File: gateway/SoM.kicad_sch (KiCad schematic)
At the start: 20 parts, among them SW901 Reset, SW902 On / Off, X901 UART, X902 SoM

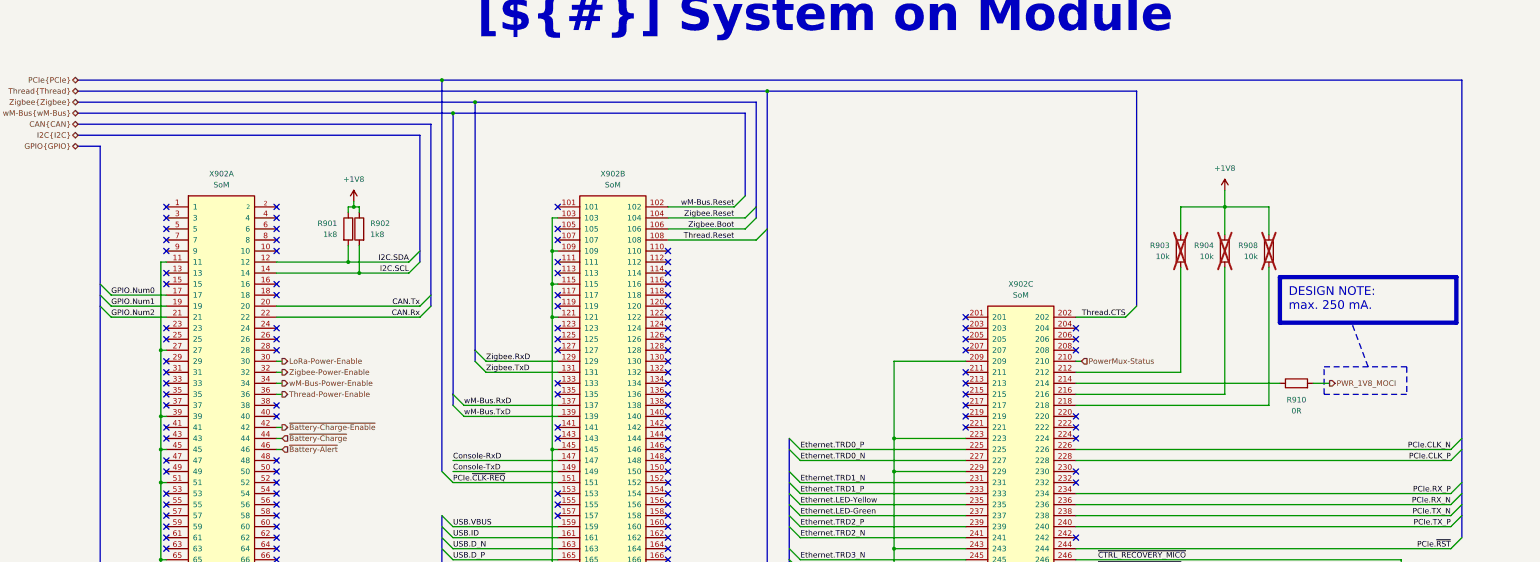
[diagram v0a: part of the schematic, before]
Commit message: Add ready LED, swap Zigbee and Console UART
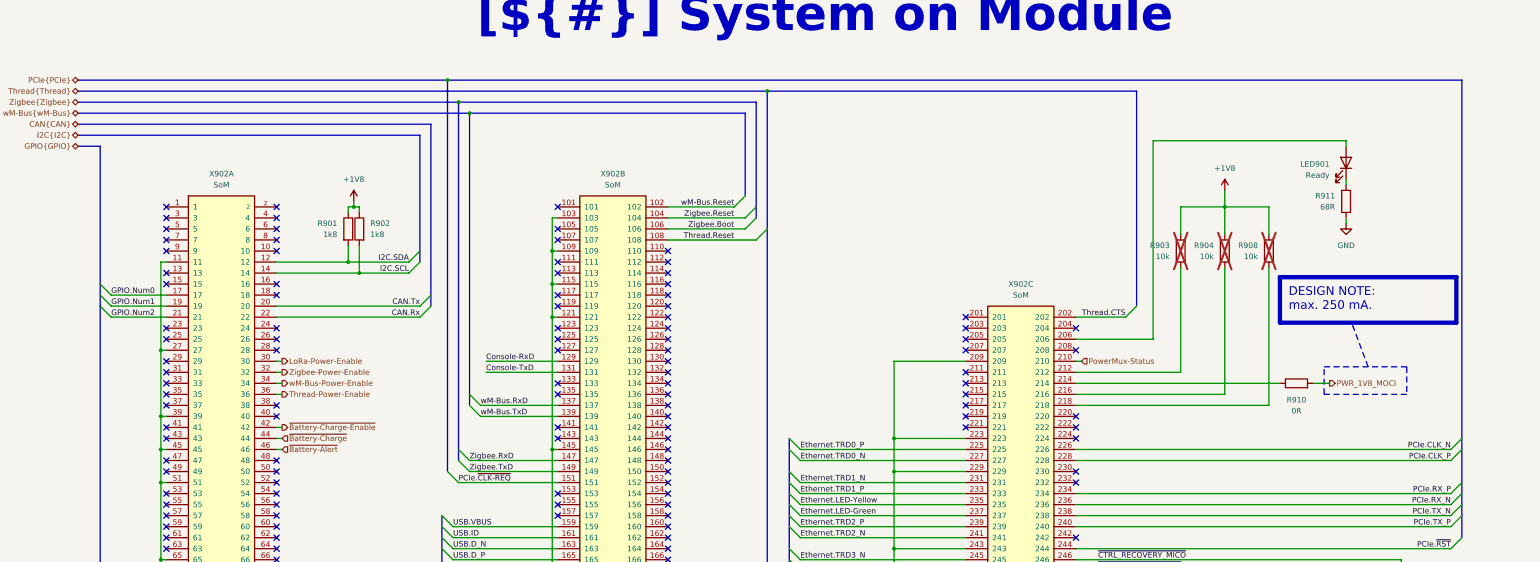
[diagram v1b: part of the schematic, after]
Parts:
- added LED901: Ready, LED_SMD:LED_0805_2012Metric, symbol Device:LED
- added R911: 68R, Resistor_SMD:R_0805_2012Metric, symbol Device:R
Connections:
- net Console-RxD: now also X902.129; no longer X902.147
- net Console-TxD: now also X902.131; no longer X902.149
- net GND: now also R911.2
- net Zigbee.RxD: now also X902.147; no longer X902.129
- net Zigbee.TxD: now also X902.149; no longer X902.131
- net at X902.206: now also LED901.2 (A)
- new net: LED901.1 (K), R911.1
- no-connect marks 159 -> 158

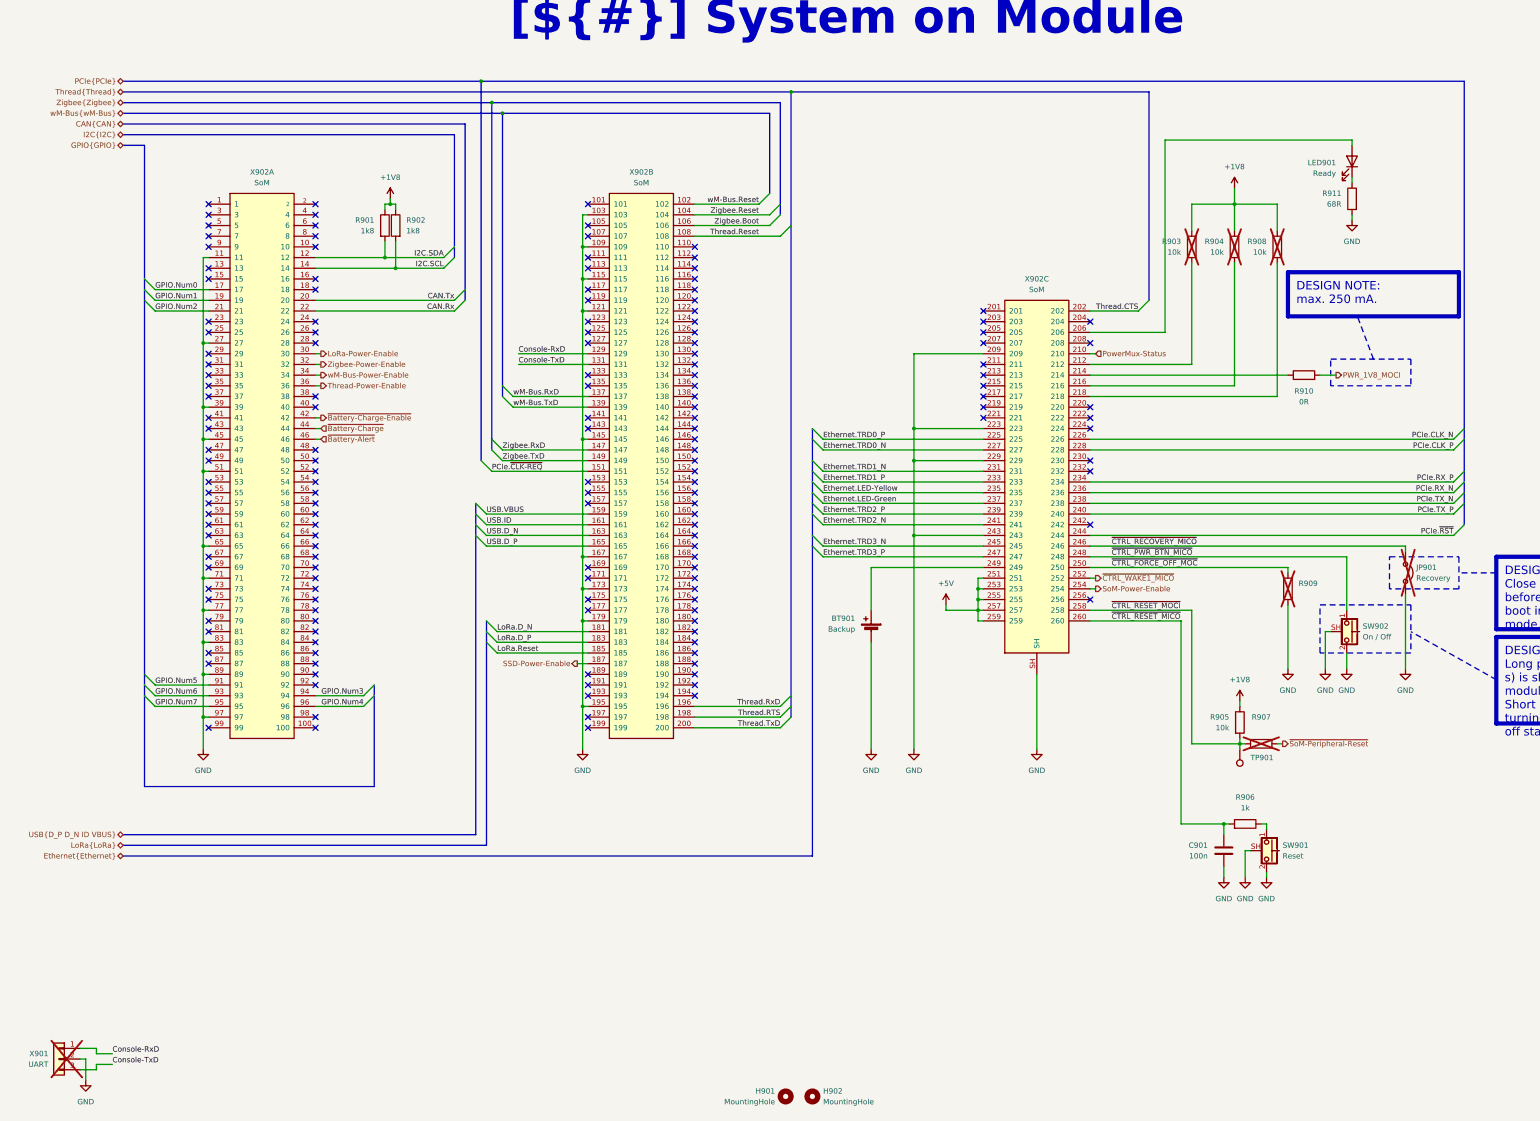
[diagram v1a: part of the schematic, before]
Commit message: Add INA219 for current measurement
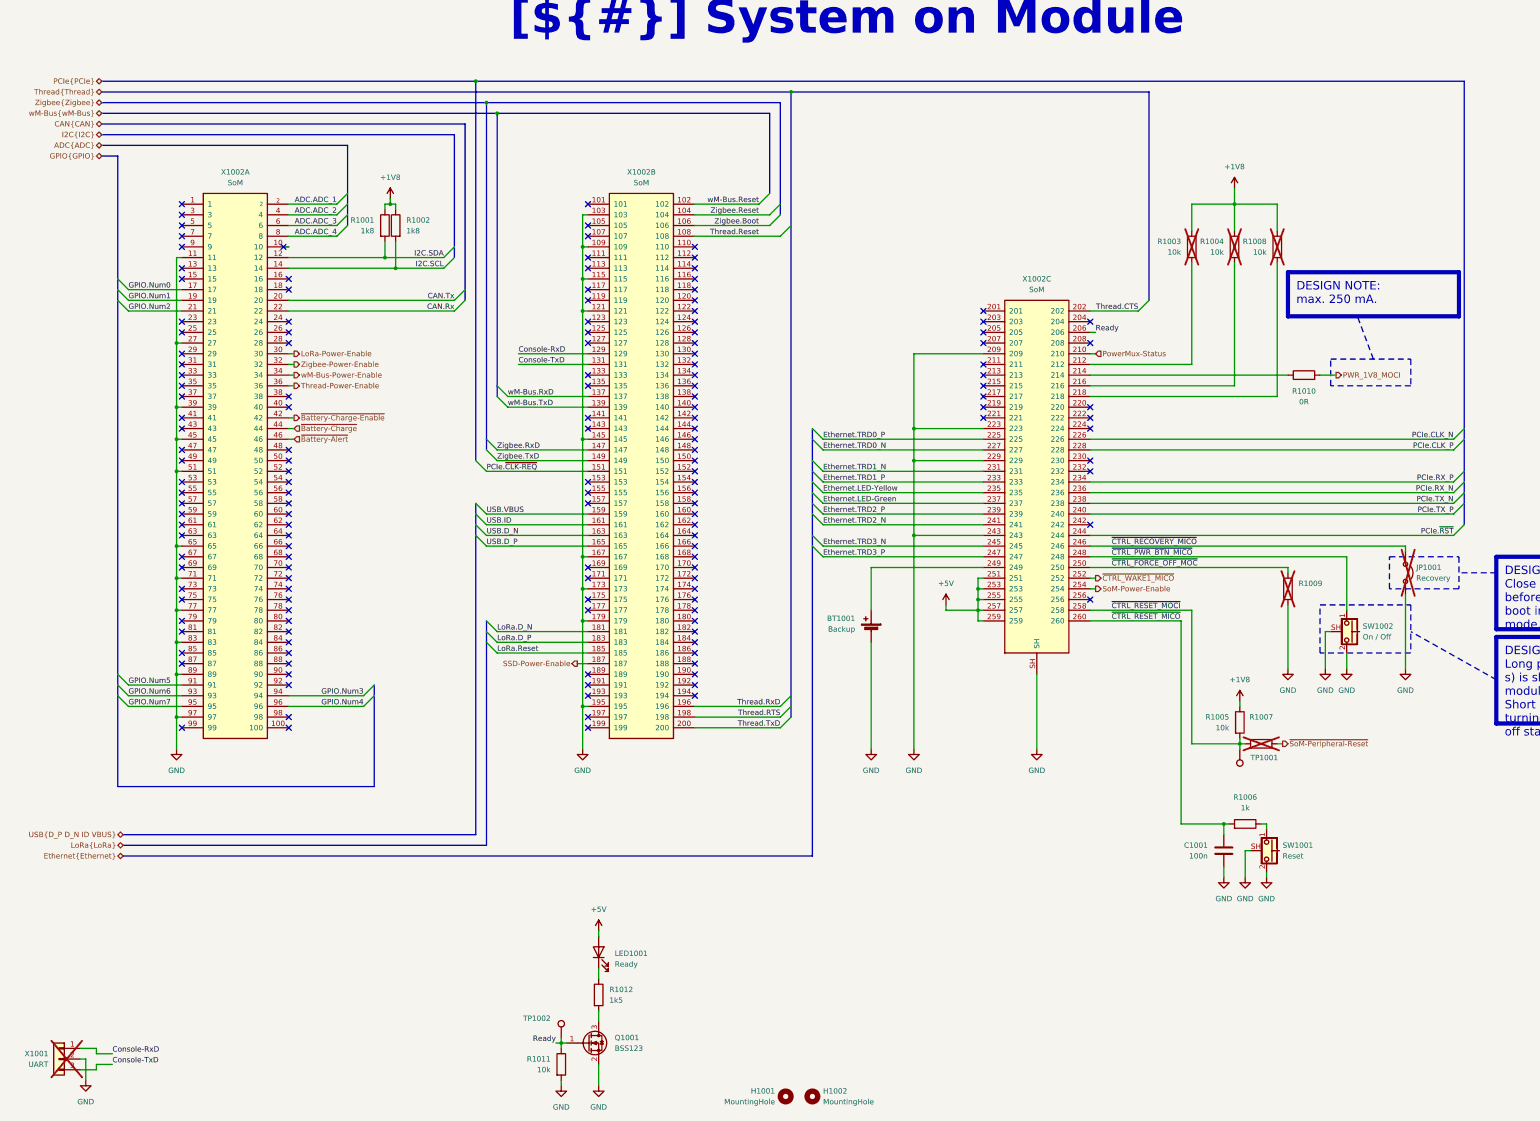
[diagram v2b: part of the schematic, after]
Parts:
- removed LED901: Ready, LED_SMD:LED_0805_2012Metric, symbol Device:LED
- removed R911: 68R, Resistor_SMD:R_0805_2012Metric, symbol Device:R
- added LED1001: Ready, LED_SMD:LED_0805_2012Metric, symbol Device:LED
- added Q1001: BSS123, Package_TO_SOT_SMD:SOT-23, symbol Transistor_FET:BSS123
- added R1011: 10k, Resistor_SMD:R_0805_2012Metric, symbol Device:R
- added R1012: 1k5, Resistor_SMD:R_0805_2012Metric, symbol Device:R
- added TP1002: ~, Testpoints_Kampi:TestPoint_Pad_1.0x1.0mm, symbol Connector:TestPoint
- renumbered BT901 to BT1001, C901 to C1001, H901 to H1001, H902 to H1002, JP901 to JP1001, R901 to R1001, R902 to R1002, R903 to R1003, R904 to R1004, R905 to R1005, R906 to R1006, R907 to R1007, R908 to R1008, R909 to R1009, R910 to R1010, SW901 to SW1001, SW902 to SW1002, TP901 to TP1001, X901 to X1001, X902 to X1002
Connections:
- net +5V: now also LED1001.2 (A)
- net GND: now also Q1001.2 (S), R1011.2
- net ADC.ADC_1: now reaches X1002.2
- net ADC.ADC_2: now reaches X1002.4
- net ADC.ADC_3: now reaches X1002.6
- net ADC.ADC_4: now reaches X1002.8
- net Ready: now reaches X1002.206
- net Ready: now also Q1001.1 (G), R1011.1, TP1002.1
- new net: Q1001.3 (D), R1012.2
- new net: LED1001.1 (K), R1012.1
- no-connect marks 158 -> 154
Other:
- moved on the sheet: X1002A

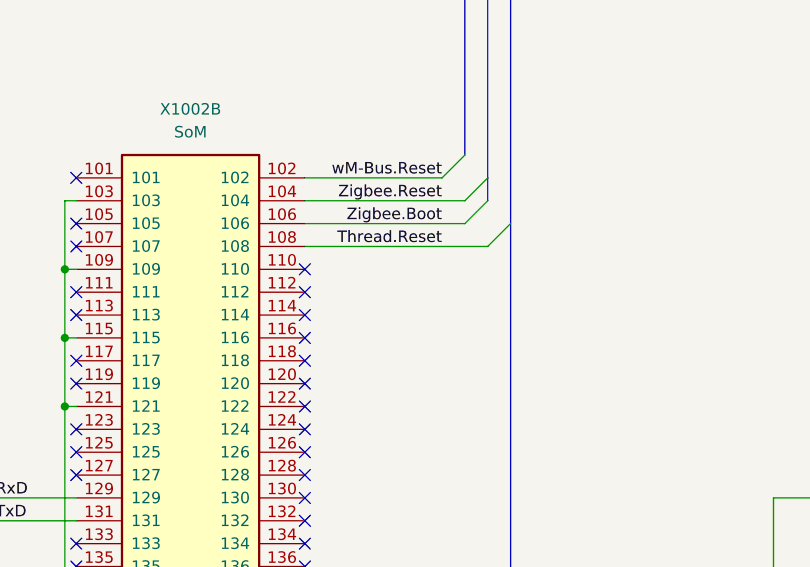
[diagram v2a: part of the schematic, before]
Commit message: Add boot signal for Thread MCU
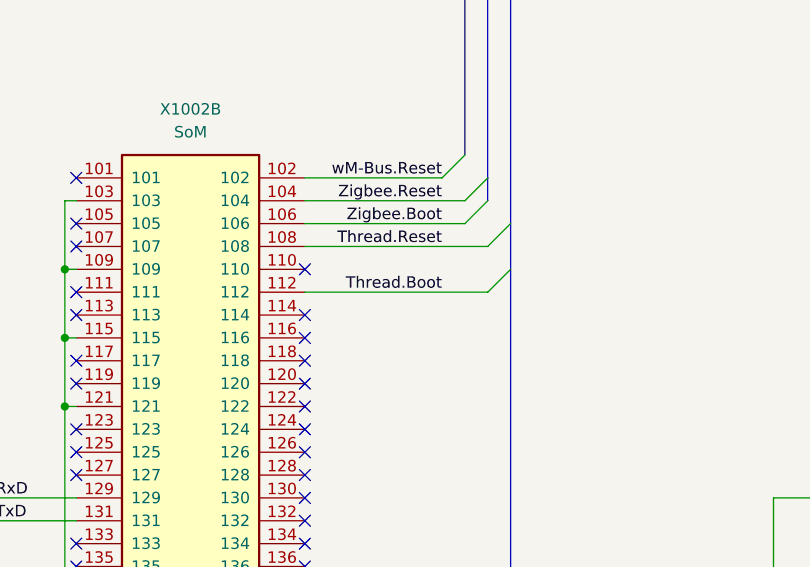
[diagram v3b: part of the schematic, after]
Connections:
- net Thread.Boot: now reaches X1002.112
- no-connect marks 154 -> 153
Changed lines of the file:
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@@
 	)
 	(no_connect
-		(at 173.99 80.01)
-	)
-	(no_connect
 		(at 52.07 118.11)
 	)
@@
 	)
 	(bus_entry
+		(at 196.85 77.47)
+		(size -2.54 2.54)
+		(stroke
+			(width 0)
+			(type default)
+		)
+	)
+	(bus_entry
 		(at 124.46 166.37)
 		(size 2.54 2.54)
@@
 	(wire
 		(pts
+			(xy 173.99 80.01) (xy 194.31 80.01)
+		)
+		(stroke
+			(width 0)
+			(type default)
+		)
+	)
+	(wire
+		(pts
 			(xy 77.47 107.95) (xy 78.74 107.95)
 		)
@@
 		)
 	)
+	(label "Thread.Boot"
+		(at 189.23 80.01 180)
+		(effects
+			(font
+				(size 1.27 1.27)
+			)
+			(justify right bottom)
+		)
+	)

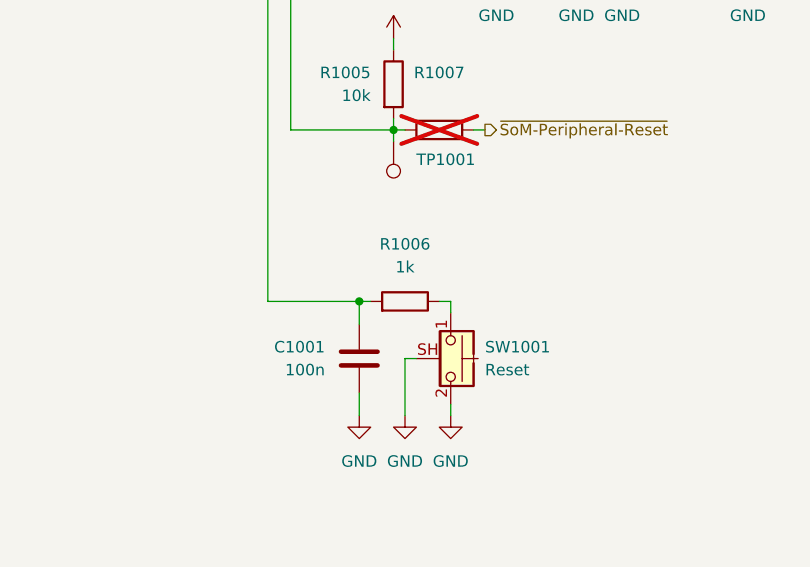
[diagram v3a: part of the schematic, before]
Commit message: Improving Thread
- Add boot signal for Thread MCU
- Add debug LED for nRF5340
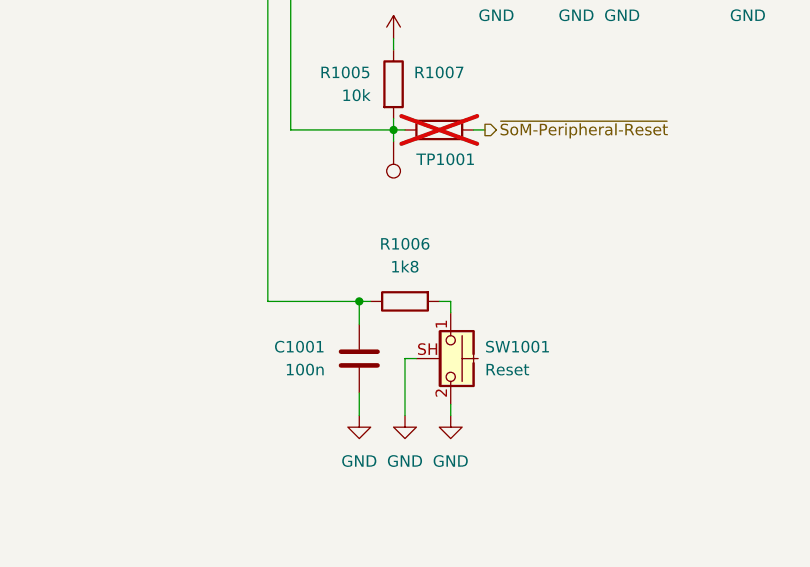
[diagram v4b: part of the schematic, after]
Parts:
- R1006: value 1k -> 1k8; manf# CR0805-FX-1001GLF -> CR0805-FX-1801GLF; mouser# 652-CR0805-FX-1001GLF -> 652-CR0805-FX-1801GLF
- TP1001, TP1002: value ~ -> (none)
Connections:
- net ~{CTRL_RESET_MICO}: now also R1006.1; no longer R1006.2
- net at SW1001.1: now also R1006.2; no longer R1006.1
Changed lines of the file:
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@@
 	)
 	(symbol
-		(lib_id "Device:R")
-		(at 304.8 214.63 270)
-		(mirror x)
-		(unit 1)
-		(body_style 1)
-		(exclude_from_sim no)
-		(in_bom yes)
-		(on_board yes)
-		(in_pos_files yes)
-		(dnp no)
-		(fields_autoplaced yes)
-		(property "Reference" "R1006"
-			(at 304.8 208.28 90)
-			(show_name no)
-			(do_not_autoplace no)
-			(effects
-				(font
-					(size 1.27 1.27)
-				)
-			)
-		)
-		(property "Value" "1k"
-			(at 304.8 210.82 90)
-			(show_name no)
-			(do_not_autoplace no)
-			(effects
-				(font
-					(size 1.27 1.27)
-				)
-			)
-		)
-		(property "Footprint" "Resistor_SMD:R_0805_2012Metric"
-			(at 304.8 216.408 90)
-			(hide yes)
-			(show_name no)
-			(do_not_autoplace no)
-			(effects
-				(font
-					(size 1.27 1.27)
-				)
-			)
-		)
-		(property "Datasheet" "https://www.mouser.de/datasheet/3/40/1/cr.pdf"
-			(at 304.8 214.63 0)
-			(hide yes)
-			(show_name no)
-			(do_not_autoplace no)
-			(effects
-				(font
-					(size 1.27 1.27)
-				)
-			)
-		)
-		(property "Description" "Resistor"
-			(at 304.8 214.63 0)
-			(hide yes)
-			(show_name no)
-			(do_not_autoplace no)
-			(effects
-				(font
-					(size 1.27 1.27)
-				)
-			)
-		)
-		(property "manf" "Bourns"
-			(at 304.8 214.63 0)
-			(hide yes)
-			(show_name no)
-			(do_not_autoplace no)
-			(effects
-				(font
-					(size 1.27 1.27)
-				)
-			)
-		)
-		(property "manf#" "CR0805-FX-1001GLF"
-			(at 304.8 214.63 0)
-			(hide yes)
-			(show_name no)
-			(do_not_autoplace no)
-			(effects
-				(font
-					(size 1.27 1.27)
-				)
-			)
-		)
-		(property "mouser#" "652-CR0805-FX-1001GLF"
-			(at 304.8 214.63 0)
-			(hide yes)
-			(show_name no)
-			(do_not_autoplace no)
-			(effects
-				(font
-					(size 1.27 1.27)
-				)
-			)
-		)
-		(pin "2"
-		)
-		(pin "1"
-		)
-		(instances
-			(project "Gateway"
-				(path "/d5742f03-3b1a-42e5-a384-018bd4b919aa/c5103ceb-5325-4a84-a025-9638a412984e/e744f3ce-03a6-44a6-8792-1447ef232b9a"
-					(reference "R1006")
-					(unit 1)
-				)
-			)
-		)
-	)
-	(symbol
 		(lib_id "Connector SODIMM:Conn_02x130_Odd_Even")
 		(at 64.77 128.27 0)
@@
 			)
 		)
-		(property "Value" "~"
+		(property "Value" ""
 			(at 139.7 263.3979 0)
 			(show_name no)
@@
 	(symbol
 		(lib_id "Device:R")
+		(at 304.8 214.63 90)
+		(mirror x)
+		(unit 1)
+		(body_style 1)
+		(exclude_from_sim no)
+		(in_bom yes)
+		(on_board yes)
+		(in_pos_files yes)
+		(dnp no)
+		(fields_autoplaced yes)
+		(property "Reference" "R1006"
+			(at 304.8 208.28 90)
+			(show_name no)
+			(do_not_autoplace no)
+			(effects
+				(font
+					(size 1.27 1.27)
+				)
+			)
+		)
+		(property "Value" "1k8"
+			(at 304.8 210.82 90)
+			(show_name no)
+			(do_not_autoplace no)
+			(effects
+				(font
+					(size 1.27 1.27)
+				)
+			)
+		)
+		(property "Footprint" "Resistor_SMD:R_0805_2012Metric"
+			(at 304.8 212.852 90)
+			(hide yes)
+			(show_name no)
+			(do_not_autoplace no)
+			(effects
+				(font
+					(size 1.27 1.27)
+				)
+			)
+		)
+		(property "Datasheet" "https://www.mouser.de/datasheet/3/40/1/cr.pdf"
+			(at 304.8 214.63 0)
+			(hide yes)
+			(show_name no)
+			(do_not_autoplace no)
+			(effects
+				(font
+					(size 1.27 1.27)
+				)
+			)
+		)
+		(property "Description" "Resistor"
+			(at 304.8 214.63 0)
+			(hide yes)
+			(show_name no)
+			(do_not_autoplace no)
+			(effects
+				(font
+					(size 1.27 1.27)
+				)
+			)
+		)
+		(property "manf" "Bourns"
+			(at 304.8 214.63 0)
+			(hide yes)
+			(show_name no)
+			(do_not_autoplace no)
+			(effects
+				(font
+					(size 1.27 1.27)
+				)
+			)
+		)
+		(property "manf#" "CR0805-FX-1801GLF"
+			(at 304.8 214.63 0)
+			(hide yes)
+			(show_name no)
+			(do_not_autoplace no)
+			(effects
+				(font
+					(size 1.27 1.27)
+				)
+			)
+		)
+		(property "mouser#" "652-CR0805-FX-1801GLF"
+			(at 304.8 214.63 0)
+			(hide yes)
+			(show_name no)
+			(do_not_autoplace no)
+			(effects
+				(font
+					(size 1.27 1.27)
+				)
+			)
+		)
+		(pin "2"
+		)
+		(pin "1"
+		)
+		(instances
+			(project "Gateway"
+				(path "/d5742f03-3b1a-42e5-a384-018bd4b919aa/c5103ceb-5325-4a84-a025-9638a412984e/e744f3ce-03a6-44a6-8792-1447ef232b9a"
+					(reference "R1006")
+					(unit 1)
+				)
+			)
+		)
+	)
+	(symbol
+		(lib_id "Device:R")
 		(at 292.1 77.47 0)
 		(unit 1)
@@
 			)
 		)
-		(property "Value" "~"
+		(property "Value" ""
 			(at 306.07 201.4219 0)
 			(show_name no)

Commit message: Working on PCB
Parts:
- added R1003: 1k8, Resistor_SMD:R_0805_2012Metric, symbol Device:R
- TP1001: renamed from TP1002; value (none) -> ~
- TP1002: renamed from TP1001; value (none) -> ~
- renumbered R1011 to R1004, R1012 to R1005, R1003 to R1006, R1004 to R1007, R1005 to R1008, R1006 to R1009, R1007 to R1010, R1008 to R1011, R1009 to R1012, R1010 to R1013
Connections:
- net +1V8: now also R1003.1
- net Input-Status: now reaches X1002.38
- net AT-DET: now reaches X1002.48
- net AT-DET: now also R1003.2
- net PowerMux-Status renamed Backup-Status
- no-connect marks 153 -> 151
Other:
- moved on the sheet: R1001, R1002
